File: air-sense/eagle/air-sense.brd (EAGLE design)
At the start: 25.3 x 71.1 mm, 6 parts

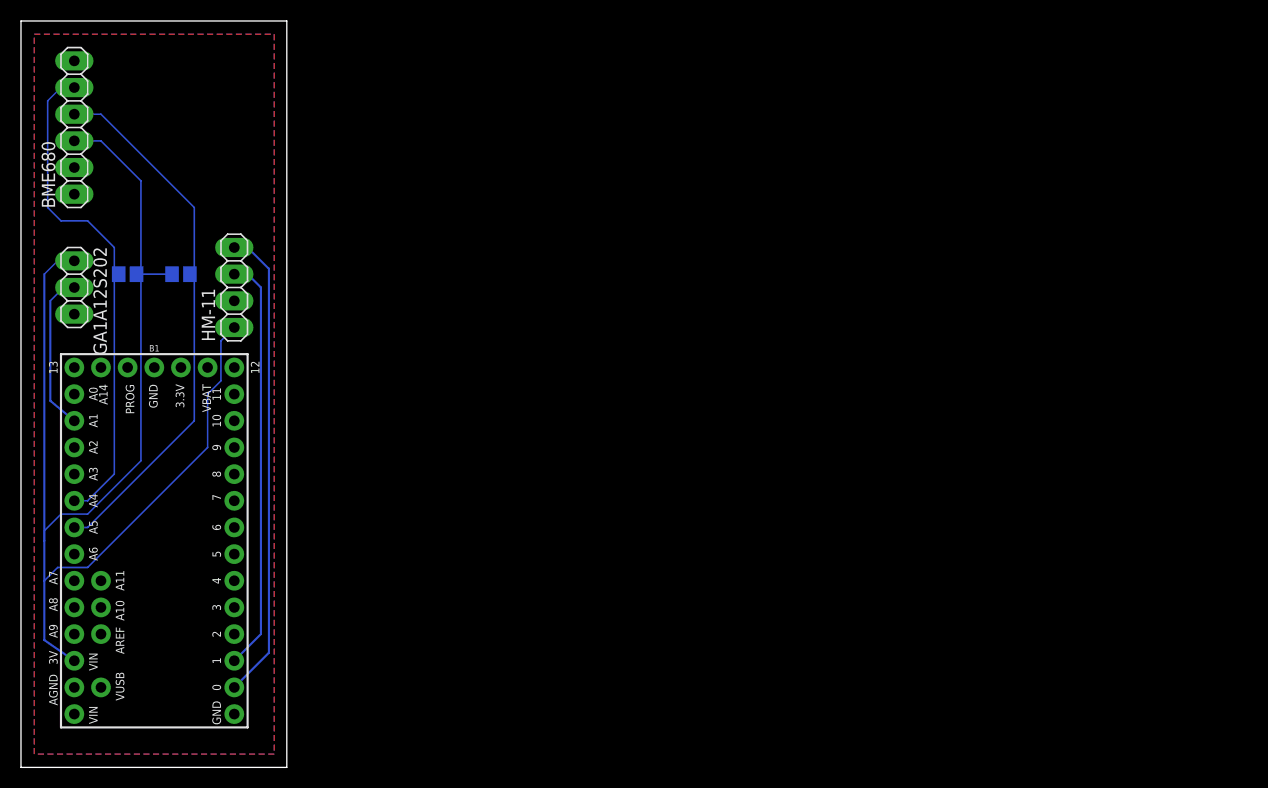
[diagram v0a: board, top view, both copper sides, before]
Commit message: Add air-sense v2 eagle files with hm-11 pads
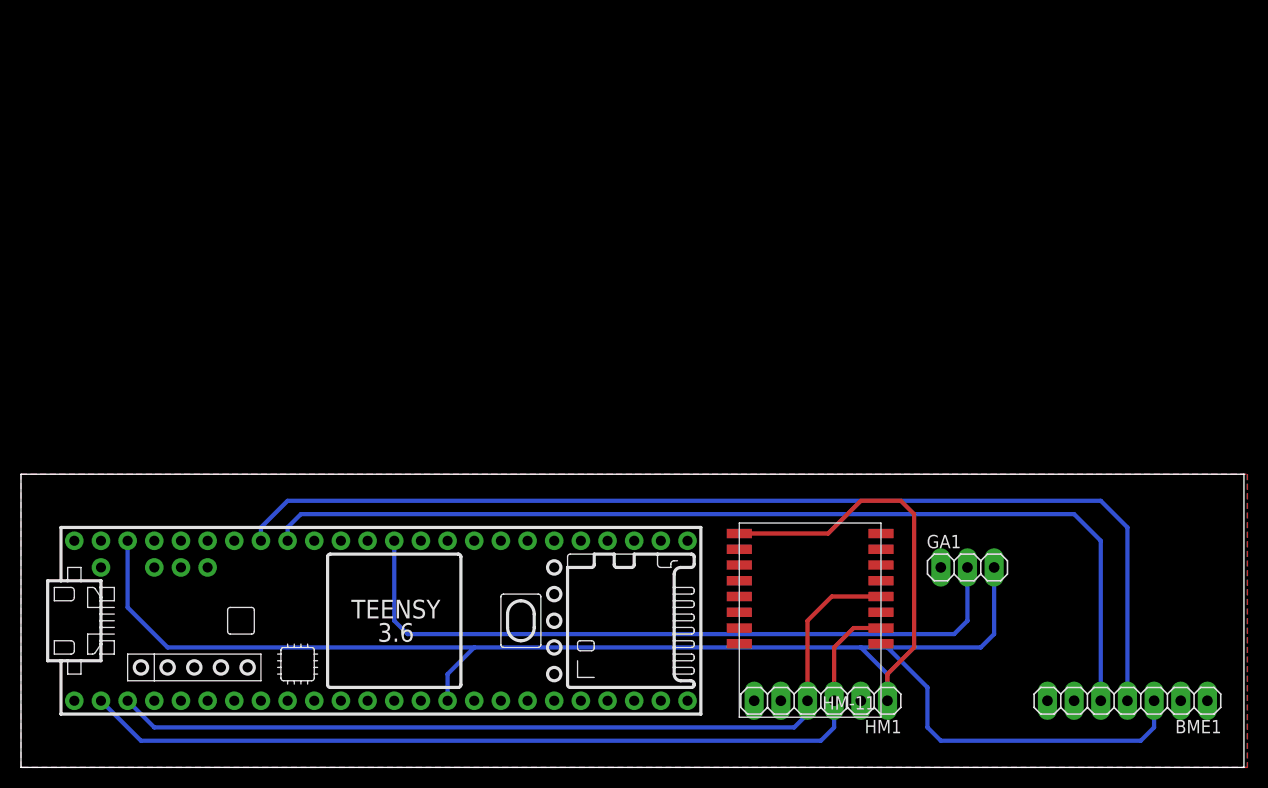
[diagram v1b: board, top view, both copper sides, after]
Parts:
- removed B1: TEENSY-3.1SILK, SparkFun-Boards:TEENSY-3.1
- removed BME680: (no value), pinhead:1X06
- removed GA1A12S202: (no value), pinhead:1X03
- removed HM-11: (no value), pinhead:1X04
- removed R1, R2: 4.7k, resistor:R2012
- added BME1: BME680-BREAKOUT, AQ-Parts:BME680-1X07
- added GA1: GA1A12S202-BREAKOUT, AQ-Parts:GA1A12S202-BREAKOUT
- added HM1: HM11-BREAKOUT, AQ-Parts:HM11-BREAKOUT
- added U$1: TEENSY_3.5/3.6_BASIC, Teensy356:TEENSY_3.5/3.6_BASIC
- added U$2: HM-11, smartwatch-hm11:HM-11
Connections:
- removed net +3V3: B1.3V, BME680.3, GA1A12S202.1, HM-11.1, R1.2, R2.2
- removed net 3.3V: B1.3.3V
- removed net AGND: B1.AGND
- removed net N$4: B1.1, HM-11.3
- removed net N$5: B1.0, HM-11.4
- removed net VBAT: B1.VBAT
- removed net VIN: B1.VIN
- removed net VUSB: B1.VUSB
- new net SCL: BME1.SCL/SCK, U$1.19/A5/SCL
- new net SDA: BME1.SDA/SDI, U$1.18/A4/SDA
- new net VCC: BME1.VCC, GA1.VCC, HM1.VCC, U$1.3V3, U$1.3V3_LO, U$2.VCC
- net GND: now also BME1.GND, GA1.GND, HM1.GND, U$1.GND, U$2.GND; no longer B1.GND, B1.GND1, BME680.1, GA1A12S202.3, HM-11.2
- net N$1: now also HM1.TX, U$1.0/RX, U$2.UART_TX; no longer B1.18, BME680.5, R2.1
- net N$2: now also HM1.RX, U$1.1/TX, U$2.UART_RX; no longer B1.19, BME680.4, R1.1
- net N$3: now also GA1.OUT, U$1.14/A0; no longer B1.15, GA1A12S202.2
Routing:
- net VCC: track 0.00 -> 181.3 mm
- net +3V3: track 126.3 -> 0.00 mm
- net SCL: track 0.00 -> 102.4 mm
- net SDA: track 0.00 -> 95.6 mm
- net N$3: track 15.3 -> 68.4 mm
- net N$5: track 45.4 -> 0.00 mm
- net N$4: track 39.7 -> 0.00 mm
- net N$1: track 48.0 -> 84.8 mm
- net N$2: track 51.4 -> 83.2 mm
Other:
- board size 25.3 x 71.1 mm -> 116.5 x 27.9 mm
